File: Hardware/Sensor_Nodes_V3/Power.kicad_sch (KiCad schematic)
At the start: 14 parts, among them U2 TPS563200, U4 AMS1117-3.3

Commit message: a lot of progress on V3, still need to test if bootloader works
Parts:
- added D6: 1N5819, Diode_SMD:D_SOD-323_HandSoldering, symbol Device:D_Schottky
- C1, C2: footprint (none) -> Capacitor_SMD:C_1206_3216Metric
- C3, C4, C5: footprint (none) -> Capacitor_SMD:C_0402_1005Metric
- C6: footprint Capacitor_SMD:C_0603_1608Metric -> Capacitor_SMD:C_0805_2012Metric
- L1: footprint (none) -> Inductor_SMD:L_Cenker_CKCS6045
- R1: value R -> 56k2; footprint (none) -> Resistor_SMD:R_0402_1005Metric
- R2: value R -> 10k; footprint (none) -> Resistor_SMD:R_0402_1005Metric
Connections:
- net Vin_D: now reaches C1.1, C2.1, U2.3 (VIN), U2.5 (EN)
- net Vin_D: now also D6.1 (K)
- new net +12V: D6.2 (A)
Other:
- moved on the sheet: C1, C2, R1, R2

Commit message: sync update
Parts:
- C1, C2: footprint Capacitor_SMD:C_1206_3216Metric -> Capacitor_SMD:C_0603_1608Metric
- C3: footprint Capacitor_SMD:C_0402_1005Metric -> Capacitor_SMD:C_0603_1608Metric
- C4, C5: footprint Capacitor_SMD:C_0402_1005Metric -> Resistor_SMD:R_0805_2012Metric
- C6: footprint Capacitor_SMD:C_0805_2012Metric -> Capacitor_SMD:C_0603_1608Metric
- R3: footprint Resistor_SMD:R_0603_1608Metric -> Resistor_SMD:R_0402_1005Metric
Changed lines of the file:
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@@
 			)
 		)
-		(property "Footprint" "Capacitor_SMD:C_1206_3216Metric"
+		(property "Footprint" "Capacitor_SMD:C_0603_1608Metric"
 			(at 22.5552 34.29 0)
 			(effects
@@
 			)
 		)
-		(property "Footprint" "Capacitor_SMD:C_0402_1005Metric"
+		(property "Footprint" "Resistor_SMD:R_0805_2012Metric"
 			(at 106.3752 34.29 0)
 			(effects
@@
 			)
 		)
-		(property "Footprint" "Capacitor_SMD:C_0402_1005Metric"
+		(property "Footprint" "Capacitor_SMD:C_0603_1608Metric"
 			(at 72.0852 31.75 0)
 			(effects
@@
 			)
 		)
-		(property "Footprint" "Capacitor_SMD:C_0805_2012Metric"
+		(property "Footprint" "Capacitor_SMD:C_0603_1608Metric"
 			(at 25.0952 71.12 0)
 			(effects
@@
 			)
 		)
-		(property "Footprint" "Resistor_SMD:R_0603_1608Metric"
+		(property "Footprint" "Resistor_SMD:R_0402_1005Metric"
 			(at 64.262 67.31 90)
 			(effects
@@
 			)
 		)
-		(property "Footprint" "Capacitor_SMD:C_0402_1005Metric"
+		(property "Footprint" "Resistor_SMD:R_0805_2012Metric"
 			(at 94.9452 34.29 0)
 			(effects
@@
 			)
 		)
-		(property "Footprint" "Capacitor_SMD:C_1206_3216Metric"
+		(property "Footprint" "Capacitor_SMD:C_0603_1608Metric"
 			(at 36.5252 34.29 0)
 			(effects

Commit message: finished the thing, need to optimize bom a little bit. need to flip some of the components too
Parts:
- C1, C2: footprint Capacitor_SMD:C_0603_1608Metric -> Capacitor_SMD:C_0805_2012Metric; LCSC (none) -> C15850
- C3: LCSC (none) -> C14663
- C4, C5: footprint Resistor_SMD:R_0805_2012Metric -> Capacitor_SMD:C_0805_2012Metric; LCSC (none) -> C45783
- C6: footprint Capacitor_SMD:C_0603_1608Metric -> Capacitor_SMD:C_0805_2012Metric; LCSC C96446 -> C15850
- C7: footprint Capacitor_SMD:C_1206_3216Metric -> Capacitor_SMD:C_0805_2012Metric; LCSC C12891 -> C45783
- D1: value LED -> RED
- L1: LCSC (none) -> C5291878
- R1: LCSC (none) -> C25796
- R2: LCSC (none) -> C25744
- R3: LCSC C22962 -> C25091
- U2: LCSC (none) -> C97253
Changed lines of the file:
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@@
 			)
 		)
-		(property "Footprint" "Capacitor_SMD:C_0603_1608Metric"
+		(property "Footprint" "Capacitor_SMD:C_0805_2012Metric"
 			(at 22.5552 34.29 0)
 			(effects
@@
 			)
 		)
+		(property "LCSC" " C15850"
+			(at 21.59 30.48 0)
+			(effects
+				(font
+					(size 1.27 1.27)
+				)
+				(hide yes)
+			)
+		)
 		(pin "1"
 		)
@@
 			)
 		)
+		(property "LCSC" "C97253"
+			(at 52.07 26.67 0)
+			(effects
+				(font
+					(size 1.27 1.27)
+				)
+				(hide yes)
+			)
+		)
 		(pin "1"
 		)
@@
 			)
 		)
-		(property "Footprint" "Capacitor_SMD:C_1206_3216Metric"
+		(property "Footprint" "Capacitor_SMD:C_0805_2012Metric"
 			(at 50.4952 71.12 0)
 			(effects
@@
 			)
 		)
-		(property "LCSC" "C12891"
+		(property "LCSC" "C45783"
 			(at 49.53 67.31 0)
 			(effects
@@
 			)
 		)
-		(property "Value" "LED"
+		(property "Value" "RED"
 			(at 59.69 63.5 0)
 			(effects
@@
 			)
 		)
-		(property "Footprint" "Resistor_SMD:R_0805_2012Metric"
+		(property "Footprint" "Capacitor_SMD:C_0805_2012Metric"
 			(at 106.3752 34.29 0)
 			(effects
@@
 			)
 		)
+		(property "LCSC" "C45783"
+			(at 105.41 30.48 0)
+			(effects
+				(font
+					(size 1.27 1.27)
+				)
+				(hide yes)
+			)
+		)
 		(pin "1"
 		)
@@
 			)
 		)
+		(property "LCSC" "C14663"
+			(at 71.12 27.94 0)
+			(effects
+				(font
+					(size 1.27 1.27)
+				)
+				(hide yes)
+			)
+		)
 		(pin "1"
 		)
@@
 			)
 		)
+		(property "LCSC" "C5291878"
+			(at 74.93 24.13 0)
+			(effects
+				(font
+					(size 1.27 1.27)
+				)
+				(hide yes)
+			)
+		)
 		(pin "1"
 		)
@@
 			)
 		)
-		(property "Footprint" "Capacitor_SMD:C_0603_1608Metric"
+		(property "Footprint" "Capacitor_SMD:C_0805_2012Metric"
 			(at 25.0952 71.12 0)
 			(effects
@@
 			)
 		)
-		(property "LCSC" "C96446"
+		(property "LCSC" " C15850"
 			(at 24.13 67.31 0)
 			(effects
@@
 			)
 		)
-		(property "LCSC" "C22962"
+		(property "LCSC" "C25091"
 			(at 66.04 67.31 0)
 			(effects
@@
 			)
 		)
+		(property "LCSC" "C25744"
+			(at 85.09 35.56 0)
+			(effects
+				(font
+					(size 1.27 1.27)
+				)
+				(hide yes)
+			)
+		)
 		(pin "1"
 		)
@@
 			)
 		)
-		(property "Footprint" "Resistor_SMD:R_0805_2012Metric"
+		(property "Footprint" "Capacitor_SMD:C_0805_2012Metric"
 			(at 94.9452 34.29 0)
 			(effects
@@
 			)
 		)
+		(property "LCSC" "C45783"
+			(at 93.98 30.48 0)
+			(effects
+				(font
+					(size 1.27 1.27)
+				)
+				(hide yes)
+			)
+		)
 		(pin "1"
 		)
@@
 			)
 		)
-		(property "Footprint" "Capacitor_SMD:C_0603_1608Metric"
+		(property "Footprint" "Capacitor_SMD:C_0805_2012Metric"
 			(at 36.5252 34.29 0)
 			(effects
@@
 			)
 		)
+		(property "LCSC" " C15850"
+			(at 35.56 30.48 0)
+			(effects
+				(font
+					(size 1.27 1.27)
+				)
+				(hide yes)
+			)
+		)
 		(pin "1"
 		)
@@
 			(at 85.09 27.94 0)
 			(effects
+				(font
+					(size 1.27 1.27)
+				)
+				(hide yes)
+			)
+		)
+		(property "LCSC" "C25796"
+			(at 85.09 27.94 0)
+			(effects

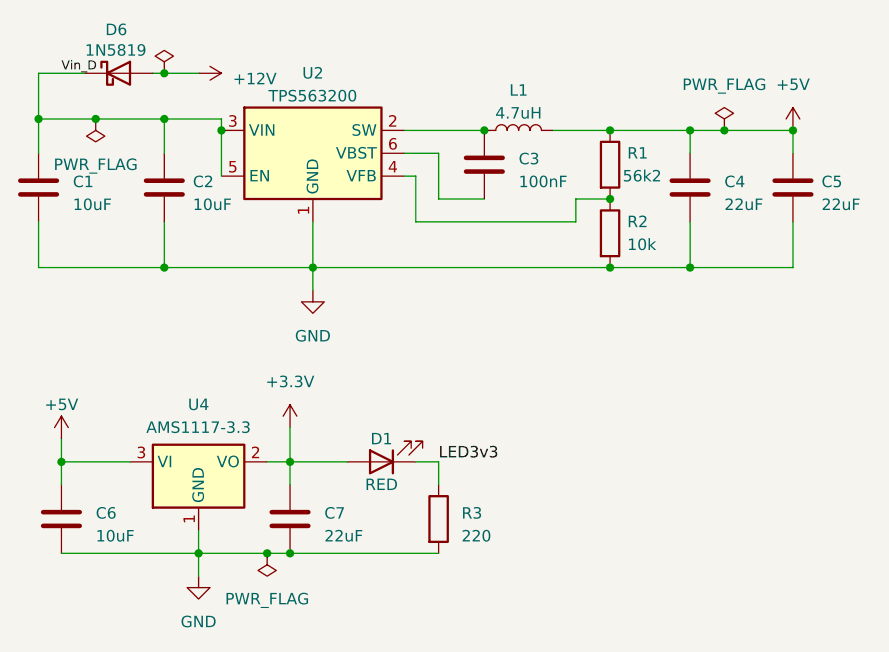
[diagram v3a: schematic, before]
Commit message: alt placement made
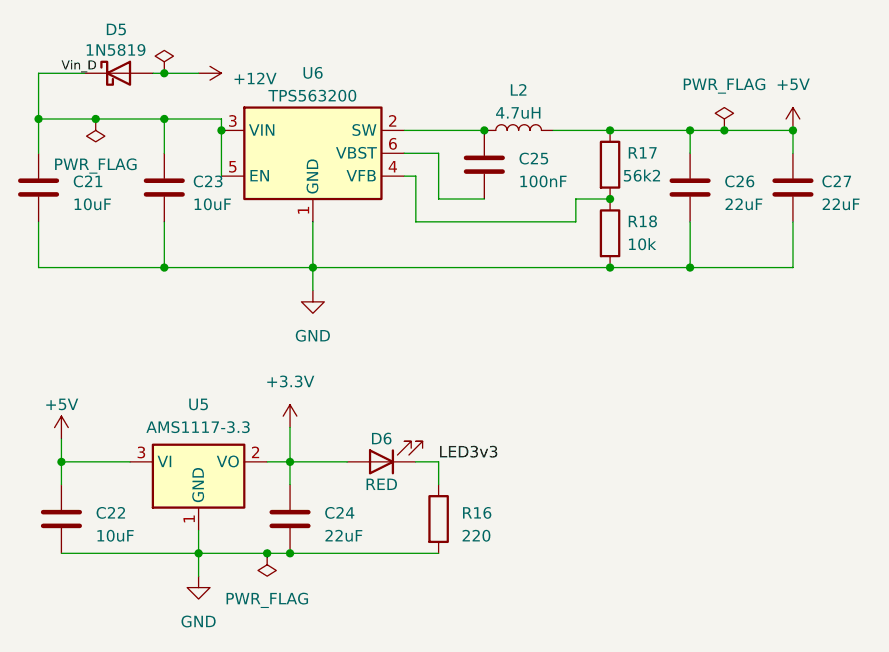
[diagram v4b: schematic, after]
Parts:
- D6: renamed from D1; footprint Diode_SMD:D_0603_1608Metric -> LED_SMD:LED_0603_1608Metric
- renumbered C1 to C21, C6 to C22, C2 to C23, C7 to C24, C3 to C25, C4 to C26, C5 to C27, D6 to D5, L1 to L2, R3 to R16, R1 to R17, R2 to R18, U4 to U5, U2 to U6
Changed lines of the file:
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@@
 		(dnp no)
 		(fields_autoplaced yes)
-		(property "Reference" "C1"
+		(property "Reference" "C21"
 			(at 25.4 29.845 0)
 			(effects
@@
 			(project "gr25_nodes"
 				(path "/7b4e8e38-4440-451f-8c12-a5c49d6e3525/ad94625e-21ee-4752-b18a-c5bc37ba7578"
-					(reference "C1")
+					(reference "C21")
 					(unit 1)
 				)
@@
 		(dnp no)
 		(fields_autoplaced yes)
-		(property "Reference" "U2"
+		(property "Reference" "U6"
 			(at 52.07 17.78 0)
 			(effects
@@
 			(project "gr25_nodes"
 				(path "/7b4e8e38-4440-451f-8c12-a5c49d6e3525/ad94625e-21ee-4752-b18a-c5bc37ba7578"
-					(reference "U2")
+					(reference "U6")
 					(unit 1)
 				)
@@
 		(dnp no)
 		(fields_autoplaced yes)
-		(property "Reference" "#PWR05"
+		(property "Reference" "#PWR053"
 			(at 49.53 60.96 0)
 			(effects
@@
 			(project ""
 				(path "/7b4e8e38-4440-451f-8c12-a5c49d6e3525/ad94625e-21ee-4752-b18a-c5bc37ba7578"
-					(reference "#PWR05")
+					(reference "#PWR053")
 					(unit 1)
 				)
@@
 		(dnp no)
 		(fields_autoplaced yes)
-		(property "Reference" "#FLG07"
+		(property "Reference" "#FLG03"
 			(at 27.94 24.765 0)
 			(effects
@@
 			(project ""
 				(path "/7b4e8e38-4440-451f-8c12-a5c49d6e3525/ad94625e-21ee-4752-b18a-c5bc37ba7578"
-					(reference "#FLG07")
+					(reference "#FLG03")
 					(unit 1)
 				)
@@
 		(dnp no)
 		(fields_autoplaced yes)
-		(property "Reference" "#PWR03"
+		(property "Reference" "#PWR050"
 			(at 24.13 62.23 0)
 			(effects
@@
 			(project "gr25_nodes"
 				(path "/7b4e8e38-4440-451f-8c12-a5c49d6e3525/ad94625e-21ee-4752-b18a-c5bc37ba7578"
-					(reference "#PWR03")
+					(reference "#PWR050")
 					(unit 1)
 				)
@@
 		(dnp no)
 		(fields_autoplaced yes)
-		(property "Reference" "#PWR01"
+		(property "Reference" "#PWR054"
 			(at 52.07 48.26 0)
 			(effects
@@
 			(project "gr25_nodes"
 				(path "/7b4e8e38-4440-451f-8c12-a5c49d6e3525/ad94625e-21ee-4752-b18a-c5bc37ba7578"
-					(reference "#PWR01")
+					(reference "#PWR054")
 					(unit 1)
 				)
@@
 		(dnp no)
 		(fields_autoplaced yes)
-		(property "Reference" "#FLG02"
+		(property "Reference" "#FLG06"
 			(at 97.79 22.225 0)
 			(effects
@@
 			(project ""
 				(path "/7b4e8e38-4440-451f-8c12-a5c49d6e3525/ad94625e-21ee-4752-b18a-c5bc37ba7578"
-					(reference "#FLG02")
+					(reference "#FLG06")
 					(unit 1)
 				)
@@
 		(dnp no)
 		(fields_autoplaced yes)
-		(property "Reference" "#PWR02"
+		(property "Reference" "#PWR055"
 			(at 105.41 27.94 0)
 			(effects
@@
 			(project ""
 				(path "/7b4e8e38-4440-451f-8c12-a5c49d6e3525/ad94625e-21ee-4752-b18a-c5bc37ba7578"
-					(reference "#PWR02")
+					(reference "#PWR055")
 					(unit 1)
 				)
@@
 		(dnp no)
 		(fields_autoplaced yes)
-		(property "Reference" "C7"
+		(property "Reference" "C24"
 			(at 53.34 66.675 0)
 			(effects
@@
 			(project "gr25_nodes"
 				(path "/7b4e8e38-4440-451f-8c12-a5c49d6e3525/ad94625e-21ee-4752-b18a-c5bc37ba7578"
-					(reference "C7")
+					(reference "C24")
 					(unit 1)
 				)
@@
 		(dnp no)
 		(fields_autoplaced yes)
-		(property "Reference" "#PWR056"
+		(property "Reference" "#PWR051"
 			(at 35.56 17.78 0)
 			(effects
@@
 			(project "gr25_nodes"
 				(path "/7b4e8e38-4440-451f-8c12-a5c49d6e3525/ad94625e-21ee-4752-b18a-c5bc37ba7578"
-					(reference "#PWR056")
+					(reference "#PWR051")
 					(unit 1)
 				)
@@
 		(on_board yes)
 		(dnp no)
-		(property "Reference" "D1"
+		(property "Reference" "D6"
 			(at 59.69 58.42 0)
 			(effects
@@
 			)
 		)
-		(property "Footprint" "Diode_SMD:D_0603_1608Metric"
+		(property "Footprint" "LED_SMD:LED_0603_1608Metric"
 			(at 59.69 60.96 0)
 			(effects
@@
 			(project "gr25_nodes"
 				(path "/7b4e8e38-4440-451f-8c12-a5c49d6e3525/ad94625e-21ee-4752-b18a-c5bc37ba7578"
-					(reference "D1")
+					(reference "D6")
 					(unit 1)
 				)
@@
 		(on_board yes)
 		(dnp no)
-		(property "Reference" "D6"
+		(property "Reference" "D5"
 			(at 30.226 12.954 0)
 			(effects
@@
 			(project "gr25_nodes"
 				(path "/7b4e8e38-4440-451f-8c12-a5c49d6e3525/ad94625e-21ee-4752-b18a-c5bc37ba7578"
-					(reference "D6")
+					(reference "D5")
 					(unit 1)
 				)
@@
 		(dnp no)
 		(fields_autoplaced yes)
-		(property "Reference" "#FLG03"
+		(property "Reference" "#FLG05"
 			(at 46.99 73.025 0)
 			(effects
@@
 			(project ""
 				(path "/7b4e8e38-4440-451f-8c12-a5c49d6e3525/ad94625e-21ee-4752-b18a-c5bc37ba7578"
-					(reference "#FLG03")
+					(reference "#FLG05")
 					(unit 1)
 				)
@@
 		(dnp no)
 		(fields_autoplaced yes)
-		(property "Reference" "U4"
+		(property "Reference" "U5"
 			(at 39.37 54.61 0)
 			(effects
@@
 			(project "gr25_nodes"
 				(path "/7b4e8e38-4440-451f-8c12-a5c49d6e3525/ad94625e-21ee-4752-b18a-c5bc37ba7578"
-					(reference "U4")
+					(reference "U5")
 					(unit 1)
 				)
@@
 		(dnp no)
 		(fields_autoplaced yes)
-		(property "Reference" "#PWR04"
+		(property "Reference" "#PWR052"
 			(at 39.37 80.01 0)
 			(effects
@@
 			(project ""
 				(path "/7b4e8e38-4440-451f-8c12-a5c49d6e3525/ad94625e-21ee-4752-b18a-c5bc37ba7578"
-					(reference "#PWR04")
+					(reference "#PWR052")
 					(unit 1)
 				)
@@
 		(dnp no)
 		(fields_autoplaced yes)
-		(property "Reference" "C5"
+		(property "Reference" "C27"
 			(at 108.585 29.845 0)
 			(effects
@@
 			(project "gr25_nodes"
 				(path "/7b4e8e38-4440-451f-8c12-a5c49d6e3525/ad94625e-21ee-4752-b18a-c5bc37ba7578"
-					(reference "C5")
+					(reference "C27")
 					(unit 1)
 				)
@@
 		(dnp no)
 		(fields_autoplaced yes)
-		(property "Reference" "C3"
+		(property "Reference" "C25"
 			(at 74.93 27.305 0)
 			(effects
@@
 			(project "gr25_nodes"
 				(path "/7b4e8e38-4440-451f-8c12-a5c49d6e3525/ad94625e-21ee-4752-b18a-c5bc37ba7578"
-					(reference "C3")
+					(reference "C25")
 					(unit 1)
 				)
@@
 		(dnp no)
 		(fields_autoplaced yes)
-		(property "Reference" "L1"
+		(property "Reference" "L2"
 			(at 74.93 19.685 90)
 			(effects
@@
 			(project "gr25_nodes"
 				(path "/7b4e8e38-4440-451f-8c12-a5c49d6e3525/ad94625e-21ee-4752-b18a-c5bc37ba7578"
-					(reference "L1")
+					(reference "L2")
 					(unit 1)
 				)
@@
 		(dnp no)
 		(fields_autoplaced yes)
-		(property "Reference" "C6"
+		(property "Reference" "C22"
 			(at 27.94 66.675 0)
 			(effects
@@
 			(project "gr25_nodes"
 				(path "/7b4e8e38-4440-451f-8c12-a5c49d6e3525/ad94625e-21ee-4752-b18a-c5bc37ba7578"
-					(reference "C6")
+					(reference "C22")
 					(unit 1)
 				)
@@
 		(dnp no)
 		(fields_autoplaced yes)
-		(property "Reference" "R3"
+		(property "Reference" "R16"
 			(at 68.58 66.675 0)
 			(effects
@@
 			(project "gr25_nodes"
 				(path "/7b4e8e38-4440-451f-8c12-a5c49d6e3525/ad94625e-21ee-4752-b18a-c5bc37ba7578"
-					(reference "R3")
+					(reference "R16")
 					(unit 1)
 				)
@@
 		(dnp no)
 		(fields_autoplaced yes)
-		(property "Reference" "R2"
+		(property "Reference" "R18"
 			(at 86.995 34.2899 0)
 			(effects
@@
 			(project "gr25_nodes"
 				(path "/7b4e8e38-4440-451f-8c12-a5c49d6e3525/ad94625e-21ee-4752-b18a-c5bc37ba7578"
-					(reference "R2")
+					(reference "R18")
 					(unit 1)
 				)
@@
 		(dnp no)
 		(fields_autoplaced yes)
-		(property "Reference" "C4"
+		(property "Reference" "C26"
 			(at 97.79 29.845 0)
 			(effects
@@
 			(project "gr25_nodes"
 				(path "/7b4e8e38-4440-451f-8c12-a5c49d6e3525/ad94625e-21ee-4752-b18a-c5bc37ba7578"
-					(reference "C4")
+					(reference "C26")
 					(unit 1)
 				)
@@
 		(dnp no)
 		(fields_autoplaced yes)
-		(property "Reference" "C2"
+		(property "Reference" "C23"
 			(at 38.735 29.845 0)
 			(effects
@@
 			(project "gr25_nodes"
 				(path "/7b4e8e38-4440-451f-8c12-a5c49d6e3525/ad94625e-21ee-4752-b18a-c5bc37ba7578"
-					(reference "C2")
+					(reference "C23")
 					(unit 1)
 				)
@@
 		(on_board yes)
 		(dnp no)
-		(property "Reference" "R1"
+		(property "Reference" "R17"
 			(at 86.995 26.6699 0)
 			(effects
@@
 			(project "gr25_nodes"
 				(path "/7b4e8e38-4440-451f-8c12-a5c49d6e3525/ad94625e-21ee-4752-b18a-c5bc37ba7578"
-					(reference "R1")
-					(unit 1)
-				)
+					(reference "R17")
+					(unit 1)
+				)

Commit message: fixed placement, added some decals, now using clock from stlink
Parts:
- L2: footprint Inductor_SMD:L_Cenker_CKCS6045 -> Inductor_SMD:L_Cenker_CKCS6020
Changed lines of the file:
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@@
 			)
 		)
-		(property "Footprint" "Inductor_SMD:L_Cenker_CKCS6045"
+		(property "Footprint" "Inductor_SMD:L_Cenker_CKCS6020"
 			(at 74.93 24.13 0)
 			(effects

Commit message: tcm can schematic done, only needs to be routed
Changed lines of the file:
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@@
 (kicad_sch
-	(version 20231120)
+	(version 20250114)
 	(generator "eeschema")
-	(generator_version "8.0")
+	(generator_version "9.0")
 	(paper "A4")
 	(junction
@@
 	(label "Vin_D"
 		(at 24.13 17.78 0)
-		(fields_autoplaced yes)
 		(effects
 			(font
@@
 	(label "LED3v3"
 		(at 66.04 60.96 0)
-		(fields_autoplaced yes)
 		(effects
 			(font
